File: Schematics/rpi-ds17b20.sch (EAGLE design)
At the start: 6 parts, among them IC1 DS18B20, IC2 DS18B20, IC3 DS18B20, IC4 DS18B20

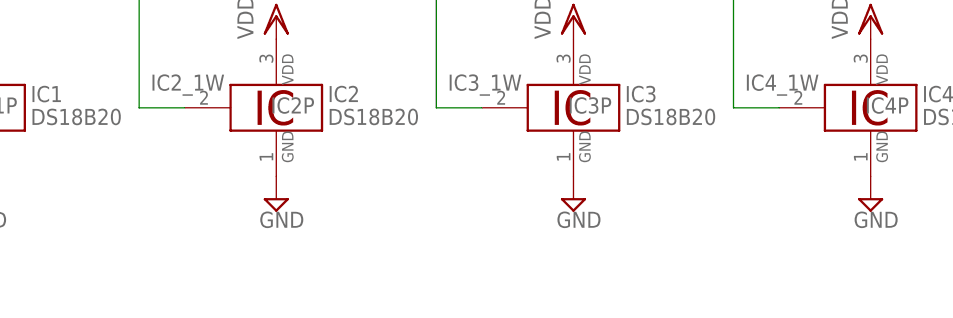
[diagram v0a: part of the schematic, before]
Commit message: add title to schematics
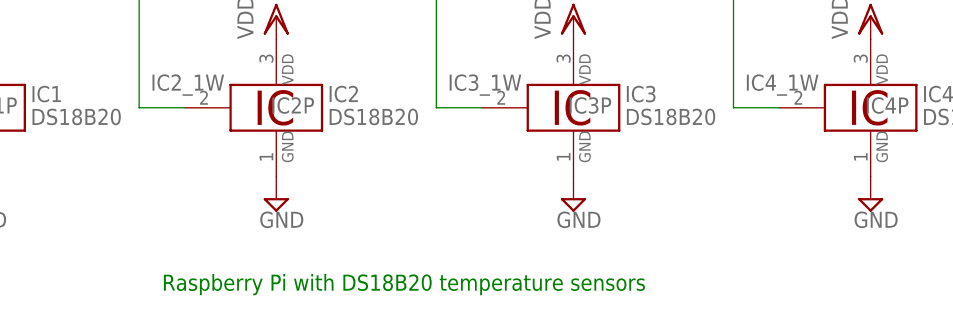
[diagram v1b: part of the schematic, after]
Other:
- note added: "Raspberry Pi with DS18B20 temperature sensors"
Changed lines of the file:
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@@
 <sheet>
 <plain>
+<text x="40.64" y="7.62" size="1.778" layer="91">Raspberry Pi with DS18B20 temperature sensors</text>
 </plain>
 <instances>
